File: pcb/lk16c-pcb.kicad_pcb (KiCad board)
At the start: 2 copper layers, 76.2 x 76.2 mm, 48 parts, among them J1 Conn_01x04, J2 Conn_01x04, J3 Conn_01x04, J4 Conn_01x04, J5 Conn_01x04, J6 Conn_01x04, J7 PINHD_1x03_ARGB, J8 PINHD_1x05_I2C, SW1 SW_Push, SW10 SW_Push, SW11 SW_Push, SW12 SW_Push, SW13 SW_Push, SW14 SW_Push, SW15 SW_Push, SW16 SW_Push, SW17 SW_Push, SW2 SW_Push, SW3 SW_Push, SW4 SW_Push, SW5 SW_Push, SW6 SW_Push, SW7 SW_Push, SW8 SW_Push, SW9 SW_Push, U1 RaspberryPi_Pico

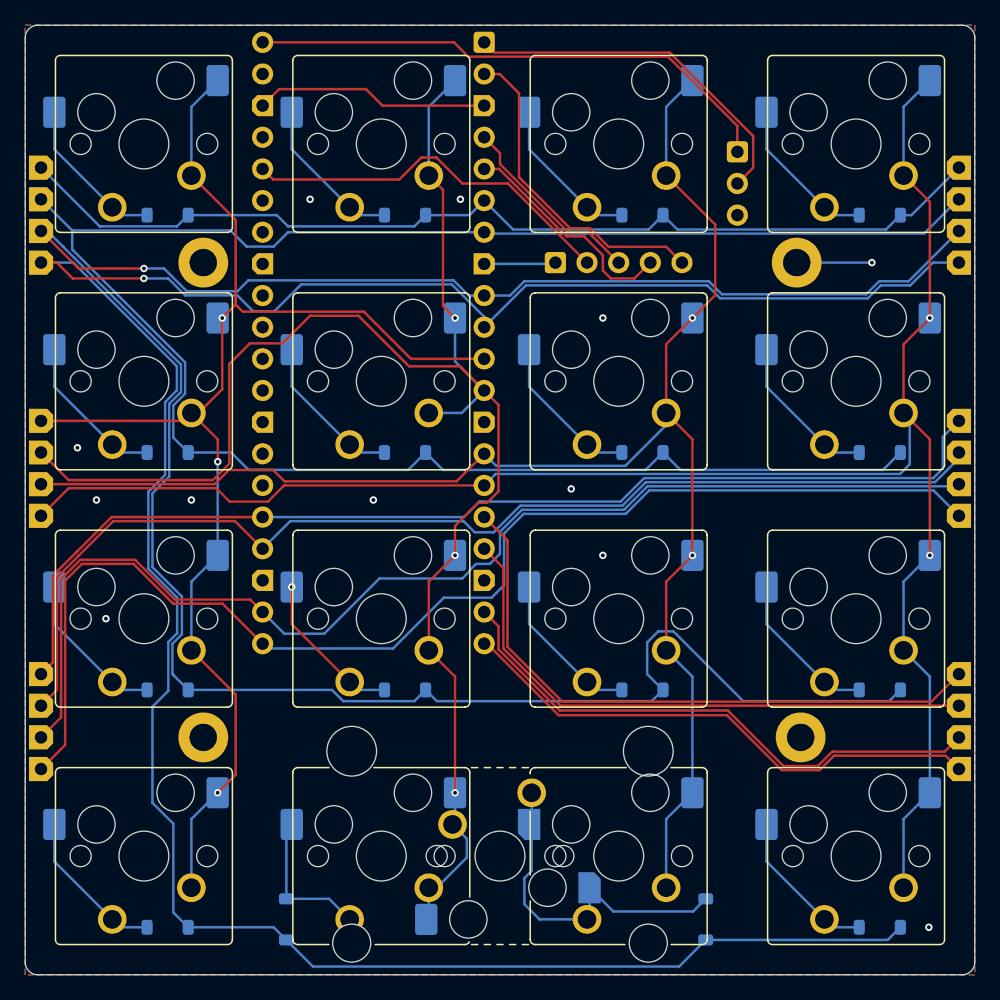
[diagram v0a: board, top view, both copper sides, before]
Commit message: Add ability to use 2× 2U Spacebars as the bottom row
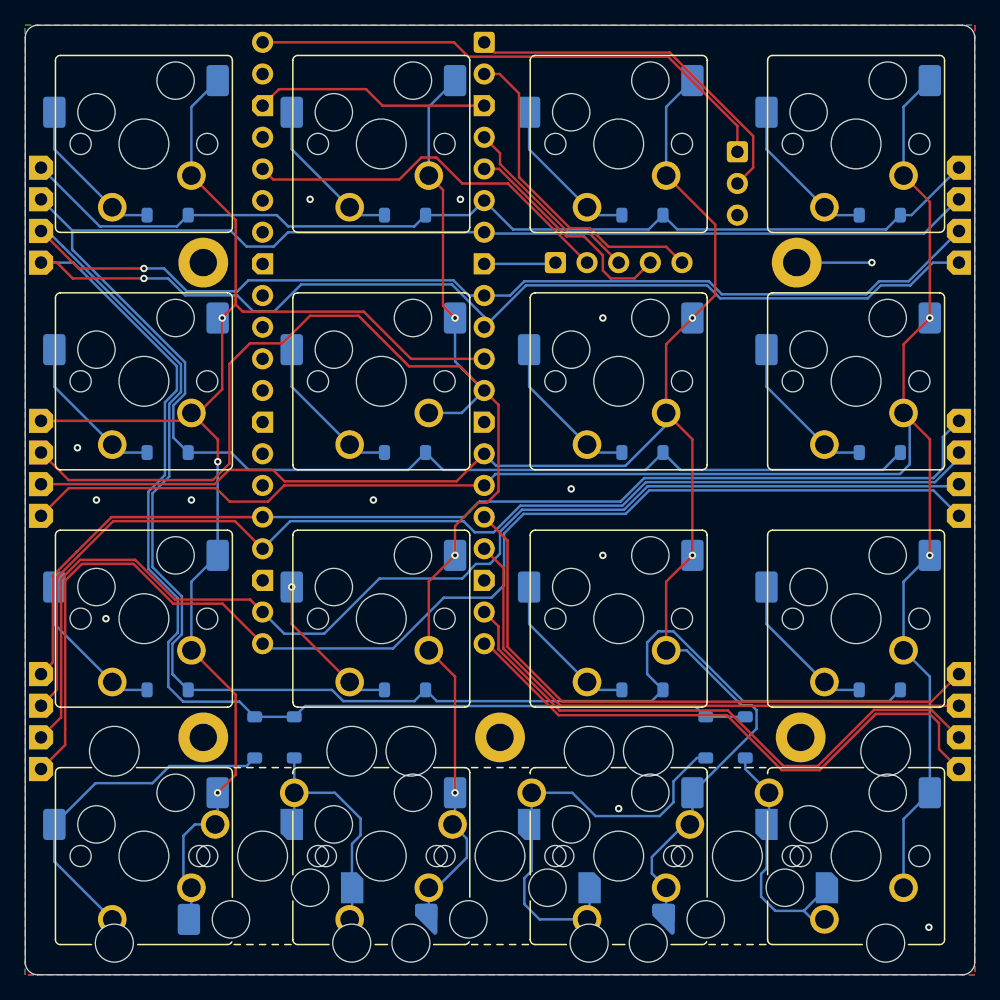
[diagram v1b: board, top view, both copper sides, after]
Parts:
- added H5: MountingHole_Pad, LKBD_MountingHole:MountingHole_M2, F.Cu at (66.7, 85.7)
- added S14: MX_stab, LKBD_StabMX:Stabilizer_MX_2U, F.Cu at (47.6, 95.2)
- added S18: MX_stab, LKBD_StabMX:Stabilizer_MX_2U, F.Cu at (85.7, 95.2)
- added SW14: SW_Push, LKBD_KeySwitch:SW_MX_Slim_HotSwap_THT_sqSilk, B.Cu at (47.6, 95.2)
- added SW18: SW_Push, LKBD_KeySwitch:SW_MX_Slim_HotSwap_THT_sqSilk, B.Cu at (85.7, 95.2)
- moved TXT1 20.4 mm to (85.7, 80.0)
- moved D19 18.7 mm to (86.4, 85.7), turned to -90 degrees
- moved D13 16.8 mm to (47.0, 85.7), turned to -90 degrees
- moved D15 14.6 mm to (50.2, 85.7), turned to -90 degrees
- moved D17 14.6 mm to (83.2, 85.7), turned to -90 degrees
- renumbered D14 to D15, D16 to D17, D17 to D19, S15 to S16, SW14 to SW15, SW15 to SW16, SW16 to SW17, SW17 to SW19
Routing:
- net /ROW4: track 204.2 -> 171.4 mm
- net Net-(D13-A): track 12.6 -> 28.7 mm
- net /COL3: track 127.1 -> 136.6 mm
- net Net-(D15-A): track 11.9 -> 20.1 mm
- net Net-(D19-A): track 12.6 -> 20.7 mm
- net Net-(D17-A): track 28.0 -> 35.2 mm
- net /COL1: track 107.7 -> 111.8 mm
- net /COL12: track 43.2 -> 47.2 mm
- net /COL11: track 45.3 -> 47.1 mm
- net GND: vias 12 -> 13
